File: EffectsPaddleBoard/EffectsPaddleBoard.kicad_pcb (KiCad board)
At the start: 4 copper layers, 114 parts, among them J1 Conn_01x03_Pin, J2 Conn_01x06_Pin, J3 Barrel_Jack, J4 Conn_01x04_Pin, J5 AudioJack2, J6 AudioJack2, SW1 SW_SPDT, SW2 SW_SPDT, SW3 SW_SPDT, U1 STM32F405RGTx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

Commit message: Reviev by David and netnaming
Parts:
- C11: footprint Capacitor_SMD:C_0402_1005Metric -> Capacitor_SMD:C_1206_3216Metric
- moved C12 206.5 mm to (230.5, 105.9)
- moved C13 206.5 mm to (230.5, 109.2)
- moved C14 206.5 mm to (230.5, 112.6)
- moved C11 200.3 mm to (230.8, 118.5)
- moved J6 178.4 mm to (258.0, 79.3)
- moved C36 156.6 mm to (180.5, 143.0)
- moved C34 153.6 mm to (177.7, 135.3)
- moved C33 152.1 mm to (173.5, 141.5)
- moved C17 147.8 mm to (179.5, 88.2)
- moved C18 147.8 mm to (179.5, 91.6)
- moved C35 146.6 mm to (170.9, 136.4)
- moved R22 146.1 mm to (178.2, 125.1)
- moved R21 143.3 mm to (171.5, 126.8)
- moved C15 143.3 mm to (170.3, 86.2)
- moved C16 143.3 mm to (170.3, 89.5)
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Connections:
- net Net-(#FLG04-pwr) renamed /Barreljack_in
- net Net-(D2-K) renamed /ph3v3out
- net Net-(D3-K) renamed /ph5vout
- net Net-(U2-BOOT) renamed /b3v3
- net Net-(U2-COMP) renamed /comp3v3
- net Net-(U2-EN) renamed /en3v3
- net Net-(U2-FB) renamed /fb3v3
- net Net-(U3-HPL) renamed /Codec/HPL
- net Net-(U3-HPR) renamed /Codec/HPR
- net Net-(U3-MIC1LM) renamed /Codec/MIC1LM
- net Net-(U3-MIC1LP) renamed /Codec/Analog_In_L
- net Net-(U3-MIC1RP) renamed /Codec/Analog_In_R
- net Net-(U3-MICBIAS) renamed /Codec/MICBIAS
- net Net-(U3-VOL/MICDET) renamed /Codec/Volume
- net Net-(U4-BOOT) renamed /b5v
- net Net-(U4-COMP) renamed /comp5v
- net Net-(U4-EN) renamed /en5v
- net Net-(U4-FB) renamed /fb5v
- U3 pad 33: unconnected-(U3-EP-Pad33) -> GND

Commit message: Proceeded in layout, just power is missing
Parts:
- C50: footprint Capacitor_SMD:C_1210_3225Metric -> Capacitor_SMD:C_1206_3216Metric
- moved C46 159.9 mm to (38.0, 190.2)
- moved C45 156.7 mm to (37.8, 184.8)
- moved R23 153.8 mm to (33.0, 192.2)
- moved U5 153.7 mm to (29.9, 178.9)
- moved C44 152.2 mm to (38.0, 178.1)
- moved C47 151.9 mm to (26.1, 186.2)
- moved R25 148.9 mm to (20.5, 187.8)
- moved C50 145.3 mm to (212.6, 106.6)
- moved R24 143.8 mm to (20.7, 180.5)
- moved R31 142.9 mm to (202.0, 105.2)
- moved R30 141.0 mm to (199.0, 105.2)
- moved R29 139.2 mm to (196.0, 105.2)
- moved RV1 138.8 mm to (197.5, 117.8), turned to 180 degrees
- moved R28 135.9 mm to (192.0, 103.7), turned to -90 degrees
- moved R27 135.5 mm to (192.0, 100.8), turned to -90 degrees
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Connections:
- net Net-(C44-Pad1) renamed /Analog_FrontBackend/InLP
- net Net-(C50-Pad1) renamed /Analog_FrontBackend/SigOutSecAmp
- net Net-(C50-Pad2) renamed /Analog_FrontBackend/AudioOutBoard
- net Net-(J5-PadT) renamed /Analog_FrontBackend/AudioInBoard
- net Net-(R30-Pad2) renamed /Analog_FrontBackend/DivAmpOut
- net Net-(U2-SS) renamed /SS3v3
- net Net-(U4-SS) renamed /SS5v
- net Net-(U5-+) renamed /Analog_FrontBackend/InSigAudio
- net Net-(U5--) renamed /Analog_FrontBackend/InFB
- net Net-(U6-+) renamed /Analog_FrontBackend/DiffIn_P
- net Net-(U6--) renamed /Analog_FrontBackend/DiffIn_N
- net Net-(U7--) renamed /Analog_FrontBackend/AmpSecIn

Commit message: Finished layout
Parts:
- removed C47: 10u, Capacitor_SMD:C_1206_3216Metric
- added D4: LED, LED_SMD:LED_0402_1005Metric, F.Cu at (155.2, 79.5)
- added R32: 220, Resistor_SMD:R_0402_1005Metric, F.Cu at (155.2, 76.8)
- moved J5 263.3 mm to (222.8, 85.5)
- moved C41 215.4 mm to (209.2, 66.0), turned to -90 degrees
- moved FB2 213.0 mm to (200.0, 65.4), turned to -90 degrees
- moved C42 212.2 mm to (205.0, 66.1), turned to -90 degrees
- moved C43 208.4 mm to (201.4, 70.4)
- moved R25 205.5 mm to (202.5, 92.4), turned to 180 degrees
- moved R24 199.1 mm to (199.3, 92.4), turned to 180 degrees
- moved R23 198.3 mm to (206.7, 96.6), turned to 180 degrees
- moved C46 194.6 mm to (204.6, 89.7), turned to -90 degrees
- moved U5 193.6 mm to (201.9, 90.0)
- moved C21 191.3 mm to (172.2, 58.5)
- moved C39 188.8 mm to (195.4, 78.2), turned to -90 degrees
- moved C27 187.2 mm to (167.1, 58.5), turned to 180 degrees
- moved C45 184.7 mm to (199.8, 96.1), turned to 90 degrees
- moved C44 184.1 mm to (202.8, 96.1), turned to 90 degrees
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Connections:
- SW2 pad 2: Net-(SW2-B) -> Codec_Reset
- U1 pad 7: Net-(SW2-B) -> Codec_Reset
- U3 pad 31: unconnected-(U3-~{RESET}-Pad31) -> Codec_Reset
- U5 pad 1: /Analog_FrontBackend/InFB -> Analog_In1
- U5 pad 4: /Analog_FrontBackend/InFB -> Analog_In1
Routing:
- added copper zone on In1.Cu, net GND
- added copper zone on In2.Cu, net GND
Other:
- board outline added: 114 x 85 mm

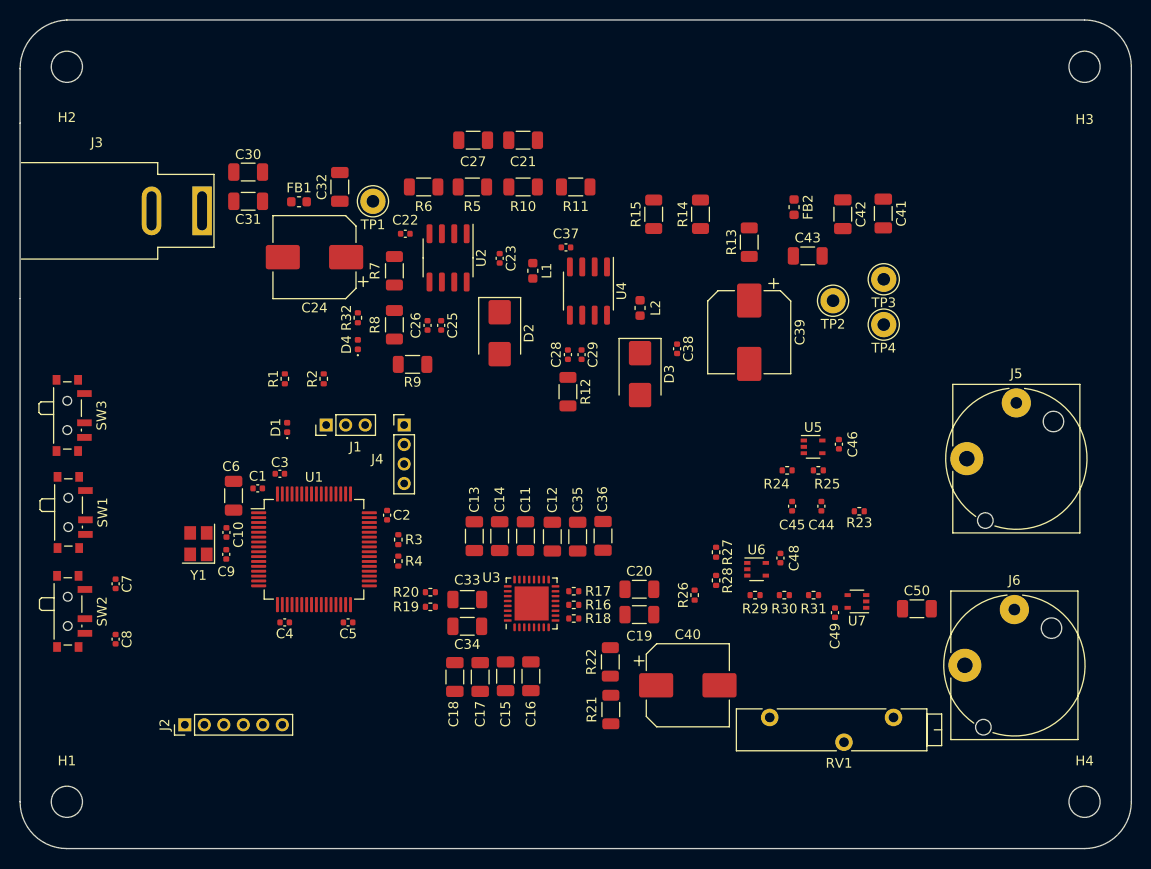
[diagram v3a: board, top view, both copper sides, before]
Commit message: Added 3d models
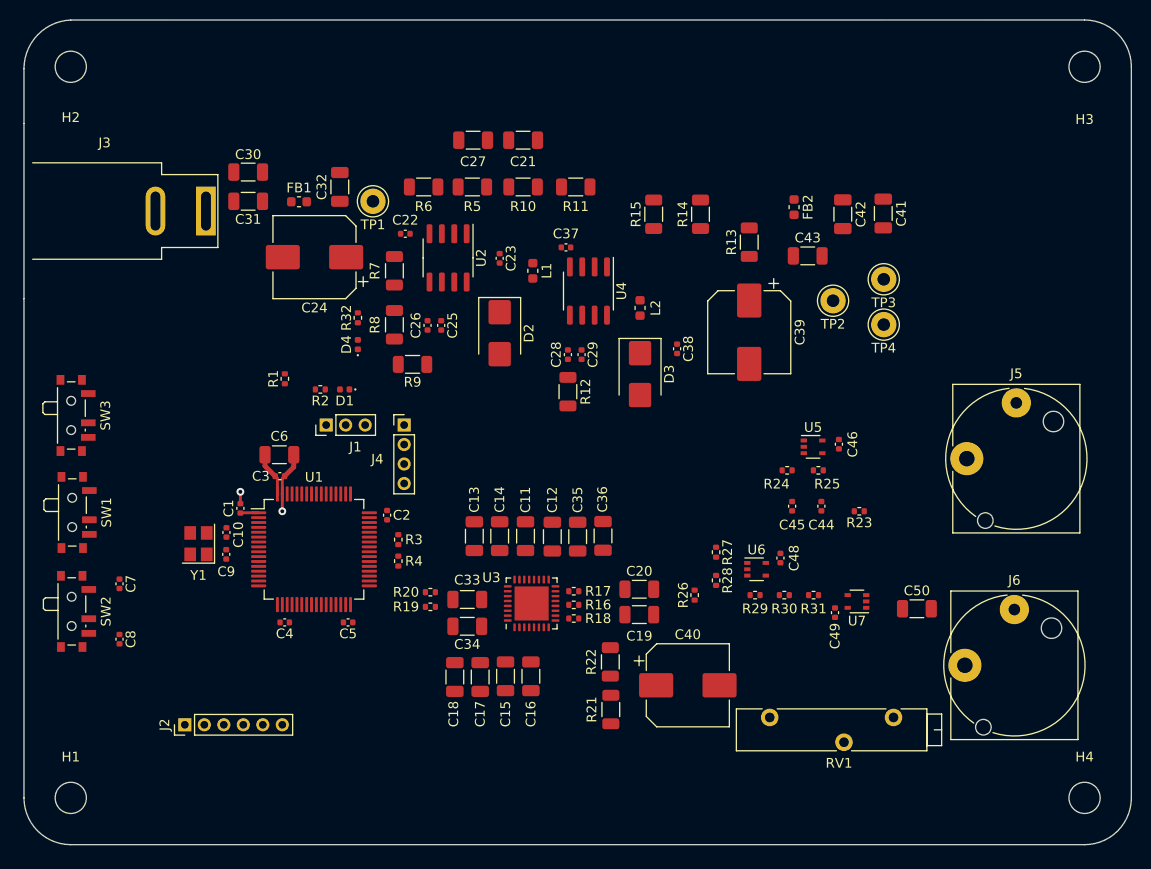
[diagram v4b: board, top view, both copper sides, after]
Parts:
- moved D1 7.07 mm to (153.9, 84.1), turned to 180 degrees
- moved C6 6.30 mm to (147.2, 90.8), turned to 0 degrees
- moved C1 2.71 mm to (143.2, 96.3), turned to 90 degrees
- moved R2 1.14 mm to (151.4, 84.1), turned to 180 degrees
- moved H1 0.57 mm to (125.8, 126.0)
- moved J3 0.40 mm to (139.7, 65.8)
- moved C7 0.40 mm to (130.8, 104.0)
- moved C8 0.40 mm to (130.8, 109.7)
- moved H4 0.40 mm to (229.8, 126.0)
- moved SW1 0.40 mm to (126.3, 96.7)
- moved SW2 0.40 mm to (126.2, 106.9)
- moved SW3 0.40 mm to (126.2, 86.8)
- moved H2 0.40 mm to (125.8, 51.0)
- moved C3 0.25 mm to (147.2, 93.0)
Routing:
- net GND: track 0.00 -> 7.51 mm, vias 0 -> 2
- net +3.3V: track 0.00 -> 6.44 mm
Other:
- board size 114 x 85 mm -> 113.6 x 84.6 mm

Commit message: Started completely new layout
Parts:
- moved H4 223.6 mm to (21.3, 45.1)
- moved H3 208.9 mm to (21.3, 37.1)
- moved J5 200.2 mm to (33.6, 20.1)
- moved J6 193.0 mm to (50.1, 20.1)
- moved U7 189.3 mm to (27.4, 44.2), turned to 0 degrees
- moved R23 186.1 mm to (31.0, 35.3), turned to 0 degrees
- moved C49 184.9 mm to (26.8, 55.0), turned to 0 degrees
- moved C50 183.3 mm to (41.1, 41.9)
- moved C44 182.7 mm to (26.8, 47.1), turned to 0 degrees
- moved U5 182.6 mm to (27.4, 36.3)
- moved C46 182.0 mm to (26.8, 51.0), turned to 0 degrees
- moved U6 179.8 mm to (27.4, 40.2)
- moved C41 179.6 mm to (32.0, 95.5), turned to 0 degrees
- moved R25 179.5 mm to (31.0, 39.3), turned to 0 degrees
- moved C45 179.3 mm to (26.8, 49.0), turned to 0 degrees
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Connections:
- U1 pad 10: I2S_ext_SD -> unconnected-(U1-PC2-Pad10)
- U1 pad 11: I2S_SD -> unconnected-(U1-PC3-Pad11)
- U1 pad 29: I2S_CK -> unconnected-(U1-PB10-Pad29)
- U1 pad 34: unconnected-(U1-PB13-Pad34) -> I2S_CK
- U1 pad 35: unconnected-(U1-PB14-Pad35) -> I2S_ext_SD
- U1 pad 36: unconnected-(U1-PB15-Pad36) -> I2S_SD
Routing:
- net I2S_MCK: track 0.00 -> 8.84 mm
- net I2S_CK: track 0.00 -> 8.26 mm, vias 0 -> 2
- net GND: track 7.51 -> 0.00 mm, vias 2 -> 0
- net I2S_WS: track 0.00 -> 6.99 mm, vias 0 -> 2
- net I2S_ext_SD: track 0.00 -> 6.52 mm, vias 0 -> 2
- net +3.3V: track 6.44 -> 0.00 mm
- net I2S_SD: track 0.00 -> 6.35 mm, vias 0 -> 2
- removed copper zone on In1.Cu, net GND
- removed copper zone on In2.Cu, net GND
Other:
- board outline removed

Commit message: Reworked schematic completely, design will be next, if someone knows, where my branches went, tell me
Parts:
- removed C49: 100n, Capacitor_SMD:C_0402_1005Metric
- removed C50: 10u, Capacitor_SMD:C_1206_3216Metric
- removed R28, R29: 4k7, Resistor_SMD:R_0402_1005Metric
- removed R30: 3k9, Resistor_SMD:R_0402_1005Metric
- removed R31: 10k, Resistor_SMD:R_0402_1005Metric
- removed RV1: 100k, Potentiometer_THT:Potentiometer_Bourns_3005_Horizontal
- removed U6, U7: MCP6401T-xLT, Package_TO_SOT_SMD:SOT-353_SC-70-5
- added C47: 1u, Capacitor_SMD:C_1206_3216Metric, F.Cu at (154.4, 108.0)
- C11, C13, C15, C17, C33, C35: value 100u -> 100n; footprint Capacitor_SMD:C_1206_3216Metric -> Capacitor_SMD:C_0603_1608Metric
- C12, C14: value 22m -> 22u
- C16, C18, C34, C36: value 10m -> 10u
- C19, C20: value 1m -> 1u
- C48: value 100n -> 1u; footprint Capacitor_SMD:C_0402_1005Metric -> Capacitor_SMD:C_1206_3216Metric
- R19: value 10k -> 0
- R27: value 3k9 -> 10k
- moved J5 149.6 mm to (142.4, 122.7)
- moved R27 137.8 mm to (145.8, 117.8)
- moved C48 135.7 mm to (152.5, 104.0)
- moved J6 133.9 mm to (159.2, 97.7), turned to 180 degrees
- moved U5 133.2 mm to (134.1, 116.0)
- moved R23 132.9 mm to (133.5, 120.0), turned to 180 degrees
- moved R24 130.9 mm to (134.1, 118.0)
- moved C44 128.2 mm to (131.9, 120.4), turned to -90 degrees
- moved R25 127.0 mm to (131.9, 116.4), turned to -90 degrees
- moved C46 126.8 mm to (136.3, 114.8), turned to 90 degrees
- moved C45 126.0 mm to (131.9, 118.4), turned to 90 degrees
- moved R26 125.8 mm to (133.2, 112.5), turned to 90 degrees
- moved C12 124.5 mm to (150.2, 113.6)
- moved C11 124.3 mm to (148.8, 111.2)
- moved C14 117.6 mm to (146.4, 114.4), turned to -90 degrees
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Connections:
- net Net-(SW2-A) renamed /uC/Boot3V3
- net Net-(SW2-C) renamed /uC/BootGND
- C48 pad 1: +5VA -> /Codec/HPR
- C48 pad 2: GND -> /Codec/HPCouplingLR
- J6 pad T: /Analog_FrontBackend/AudioOutBoard -> /Codec/HeadphonesOut
- R19 pad 1: /Codec/HPR -> /Codec/HeadphonesOut
- R19 pad 2: GND -> /Codec/HPCouplingLR
- R20 pad 1: /Codec/HPL -> /Codec/SPKL
- R27 pad 1: Audio_P -> /Codec/SPKR
- R27 pad 2: /Analog_FrontBackend/DiffIn_P -> GND
- U3 pad 19: Audio_M -> /Codec/SPKR
- U3 pad 22: Audio_P -> /Codec/SPKL
- U3 pad 23: Audio_M -> /Codec/SPKR
- U3 pad 26: Audio_P -> /Codec/SPKL
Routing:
- net I2S_MCK: track 8.84 -> 0.00 mm
- net I2S_CK: track 8.26 -> 0.00 mm, vias 2 -> 0
- net I2S_WS: track 6.99 -> 0.00 mm, vias 2 -> 0
- net I2S_ext_SD: track 6.52 -> 0.00 mm, vias 2 -> 0
- net I2S_SD: track 6.35 -> 0.00 mm, vias 2 -> 0
